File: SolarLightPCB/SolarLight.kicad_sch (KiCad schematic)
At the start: 19 parts, among them J1 I2C, J2 SPI, J3 SCK Jumper, J4 ADC, U1 TP4056, U2 WeMos_D1_mini, U3 L78L33_TO92

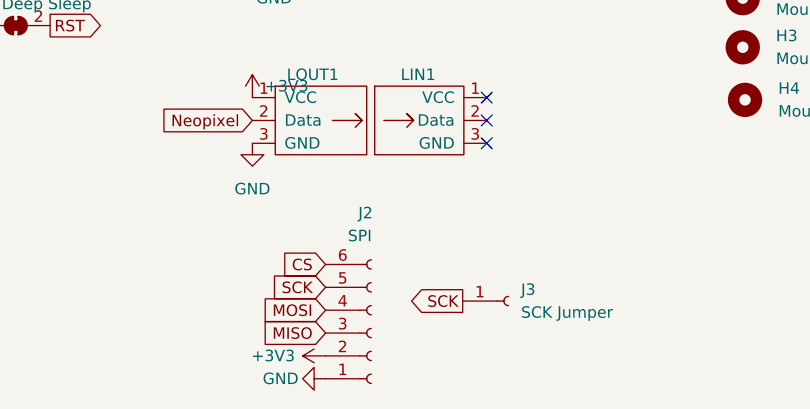
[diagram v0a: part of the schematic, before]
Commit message: Replace the missing connection with a jumper
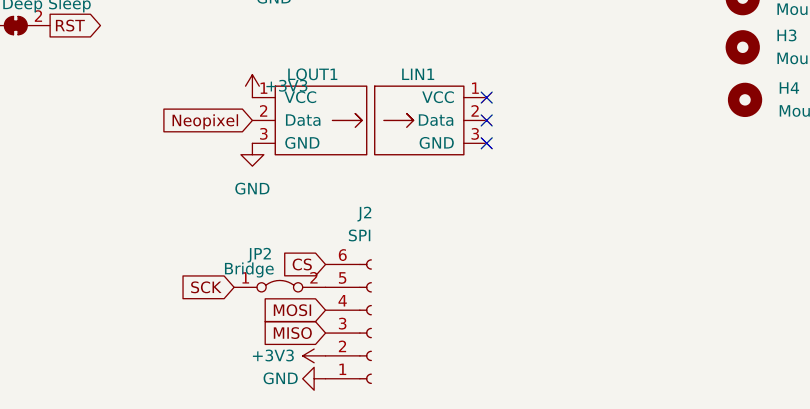
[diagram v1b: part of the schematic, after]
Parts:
- removed J3: SCK Jumper, Connector_PinHeader_2.54mm:PinHeader_1x01_P2.54mm_Vertical, symbol Connector:Conn_01x01_Female
- added JP2: Bridge, Resistor_THT:R_Box_L8.4mm_W2.5mm_P5.08mm, symbol Jumper:Jumper_2_Bridged
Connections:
- net SCK: now also JP2.1 (A); no longer J2.5 (Pin_5)
- new net: J2.5 (Pin_5), JP2.2 (B)
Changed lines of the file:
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@@
-    )
-  )
-  (global_label "SCK" (shape output) (at 234.823 117.602 180) (fields_autoplaced)
-    (effects (font (size 1.27 1.27)) (justify right))
-    (property "Intersheet References" "${INTERSHEET_REFS}" (id 0) (at 228.6604 117.6814 0)
-      (effects (font (size 1.27 1.27)) (justify right) hide)
     )
   )
@@
     )
   )
-  (global_label "SCK" (shape input) (at 219.583 116.078 180) (fields_autoplaced)
+  (global_label "SCK" (shape input) (at 209.423 116.078 180) (fields_autoplaced)
     (effects (font (size 1.27 1.27)) (justify right))
-    (property "Intersheet References" "${INTERSHEET_REFS}" (id 0) (at 213.4204 115.9986 0)
+    (property "Intersheet References" "${INTERSHEET_REFS}" (id 0) (at 203.2604 115.9986 0)
       (effects (font (size 1.27 1.27)) (justify right) hide)
     )
@@
     )
     (pin "1")
+  )
+  (symbol (lib_id "Jumper:Jumper_2_Bridged") (at 214.503 116.078 0) (unit 1)
+    (in_bom yes) (on_board yes)
+    (property "Reference" "JP2" (id 0) (at 212.344 112.395 0))
+    (property "Value" "Bridge" (id 1) (at 211.074 114.046 0))
+    (property "Footprint" "Resistor_THT:R_Box_L8.4mm_W2.5mm_P5.08mm" (id 2) (at 214.503 116.078 0)
+      (effects (font (size 1.27 1.27)) hide)
+    )
+    (property "Datasheet" "~" (id 3) (at 214.503 116.078 0)
+      (effects (font (size 1.27 1.27)) hide)
+    )
+    (pin "1")
+    (pin "2")
   )
   (symbol (lib_id "Mechanical:MountingHole") (at 265.938 83.947 0) (unit 1)
@@
     (pin "3")
   )
-  (symbol (lib_id "Connector:Conn_01x01_Female") (at 239.903 117.602 0) (unit 1)
-    (in_bom yes) (on_board yes)
-    (property "Reference" "J3" (id 0) (at 241.3 116.3319 0)
-      (effects (font (size 1.27 1.27)) (justify left))
-    )
-    (property "Value" "SCK Jumper" (id 1) (at 241.3 118.8719 0)
-      (effects (font (size 1.27 1.27)) (justify left))
-    )
-    (property "Footprint" "Connector_PinHeader_2.54mm:PinHeader_1x01_P2.54mm_Vertical" (id 2) (at 239.903 117.602 0)
-      (effects (font (size 1.27 1.27)) hide)
-    )
-    (property "Datasheet" "~" (id 3) (at 239.903 117.602 0)
-      (effects (font (size 1.27 1.27)) hide)
-    )
-    (pin "1")
-  )
   (symbol (lib_id "Device:C_Polarized") (at 146.685 33.02 0) (unit 1)
     (in_bom yes) (on_board yes) (fields_autoplaced)
@@
       (reference "J2") (unit 1) (value "SPI") (footprint "Connector_PinHeader_2.54mm:PinHeader_1x06_P2.54mm_Vertical")
     )
-    (path "/e53f4b10-ac86-4ea2-bd5b-912502e02f22"
-      (reference "J3") (unit 1) (value "SCK Jumper") (footprint "Connector_PinHeader_2.54mm:PinHeader_1x01_P2.54mm_Vertical")
-    )
     (path "/ba03d50b-1a69-484f-aaa5-388057035199"
       (reference "J4") (unit 1) (value "ADC") (footprint "Connector_PinHeader_2.54mm:PinHeader_1x01_P2.54mm_Vertical")
@@
       (reference "JP1") (unit 1) (value "Deep Sleep") (footprint "Jumper:SolderJumper-2_P1.3mm_Bridged_Pad1.0x1.5mm")
     )
+    (path "/a04ab534-b3ff-41d2-b40f-b10866f1afa8"
+      (reference "JP2") (unit 1) (value "Bridge") (footprint "Resistor_THT:R_Box_L8.4mm_W2.5mm_P5.08mm")
+    )
     (path "/efe1edb9-34c9-473f-839b-20e06ddf294c"

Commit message: Update schematic
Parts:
- U3: value L78L33_TO92 -> MCP1700-3302E
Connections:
- net ADC: no longer names the net of J4.1 (Pin_1), U2.2 (A0)
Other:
- company: (none) -> Fablab Zürich / Beat Besmer / Bernd Heistercamp
- title: (none) -> Solar Light
- moved on the sheet: J4
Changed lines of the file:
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@@
 (kicad_sch (version 20211123) (generator eeschema)
   (paper "A4")
+  (title_block
+    (title "Solar Light")
+    (date "2022-10-23")
+    (rev "v0.1")
+    (company "Fablab Zürich / Beat Besmer / Bernd Heistercamp")
+  )
   (junction (at 74.93 40.64) (diameter 0) (color 0 0 0 0)
   )
@@
     )
   )
-  (global_label "ADC" (shape output) (at 169.926 67.056 180) (fields_autoplaced)
-    (effects (font (size 1.27 1.27)) (justify right))
-    (property "Intersheet References" "${INTERSHEET_REFS}" (id 0) (at 163.8843 66.9766 0)
-      (effects (font (size 1.27 1.27)) (justify right) hide)
-    )
-  )
   (global_label "CS" (shape input) (at 219.583 113.538 180) (fields_autoplaced)
     (effects (font (size 1.27 1.27)) (justify right))
@@
     )
   )
-  (global_label "ADC" (shape input) (at 171.45 84.455 0) (fields_autoplaced)
-    (effects (font (size 1.27 1.27)) (justify left))
-    (property "Intersheet References" "${INTERSHEET_REFS}" (id 0) (at 177.4917 84.3756 0)
-      (effects (font (size 1.27 1.27)) (justify left) hide)
-    )
-  )
   (global_label "Neopixel" (shape input) (at 211.455 97.536 180) (fields_autoplaced)
     (effects (font (size 1.27 1.27)) (justify right))
@@
   (symbol (lib_id "Device:Battery_Cell") (at 118.745 38.1 0) (unit 1)
     (in_bom yes) (on_board yes)
-    (property "Reference" "BT1" (id 0) (at 122.555 34.7979 0)
+    (property "Reference" "BT1" (id 0) (at 119.507 39.116 0)
       (effects (font (size 1.27 1.27)) (justify left))
     )
     (property "Value" "Battery_Cell" (id 1) (at 113.03 42.545 0)
-      (effects (font (size 1.27 1.27)) (justify left))
+      (effects (font (size 1.27 1.27)) (justify left) hide)
     )
     (property "Footprint" "Resistor_THT:R_Axial_DIN0207_L6.3mm_D2.5mm_P10.16mm_Horizontal" (id 2) (at 118.745 36.576 90)
@@
   )
   (symbol (lib_id "Device:Solar_Cell") (at 74.93 36.83 0) (unit 1)
-    (in_bom yes) (on_board yes) (fields_autoplaced)
+    (in_bom yes) (on_board yes)
     (property "Reference" "SC1" (id 0) (at 78.74 33.4009 0)
-      (effects (font (size 1.27 1.27)) (justify left))
-    )
-    (property "Value" "Solar_Cell" (id 1) (at 78.74 35.9409 0)
+      (effects (font (size 1.27 1.27)) (justify left) hide)
+    )
+    (property "Value" "Solar_Cell" (id 1) (at 63.627 37.846 0)
       (effects (font (size 1.27 1.27)) (justify left))
     )
@@
   )
   (symbol (lib_id "power:+3V3") (at 139.7 30.48 0) (unit 1)
-    (in_bom yes) (on_board yes) (fields_autoplaced)
+    (in_bom yes) (on_board yes)
     (property "Reference" "#PWR0104" (id 0) (at 139.7 34.29 0)
       (effects (font (size 1.27 1.27)) hide)
     )
-    (property "Value" "+3V3" (id 1) (at 139.7 25.4 0))
+    (property "Value" "+3V3" (id 1) (at 142.494 27.686 0))
     (property "Footprint" "" (id 2) (at 139.7 30.48 0)
       (effects (font (size 1.27 1.27)) hide)
@@
   )
   (symbol (lib_id "Regulator_Linear:L78L33_TO92") (at 132.08 30.48 0) (unit 1)
-    (in_bom yes) (on_board yes) (fields_autoplaced)
-    (property "Reference" "U3" (id 0) (at 132.08 22.86 0))
-    (property "Value" "L78L33_TO92" (id 1) (at 132.08 25.4 0))
+    (in_bom yes) (on_board yes)
+    (property "Reference" "U3" (id 0) (at 132.08 27.432 0))
+    (property "Value" "MCP1700-3302E" (id 1) (at 132.08 25.4 0))
     (property "Footprint" "Package_TO_SOT_THT:TO-92_Inline" (id 2) (at 132.08 24.765 0)
       (effects (font (size 1.27 1.27) italic) hide)
@@
     (pin "4")
   )
-  (symbol (lib_id "Connector:Conn_01x01_Female") (at 175.006 67.056 0) (unit 1)
-    (in_bom yes) (on_board yes)
-    (property "Reference" "J4" (id 0) (at 176.403 65.7859 0)
-      (effects (font (size 1.27 1.27)) (justify left))
-    )
-    (property "Value" "ADC" (id 1) (at 176.403 68.3259 0)
-      (effects (font (size 1.27 1.27)) (justify left))
-    )
-    (property "Footprint" "Connector_PinHeader_2.54mm:PinHeader_1x01_P2.54mm_Vertical" (id 2) (at 175.006 67.056 0)
-      (effects (font (size 1.27 1.27)) hide)
-    )
-    (property "Datasheet" "~" (id 3) (at 175.006 67.056 0)
+  (symbol (lib_id "Connector:Conn_01x01_Female") (at 176.53 84.455 0) (unit 1)
+    (in_bom yes) (on_board yes)
+    (property "Reference" "J4" (id 0) (at 175.641 80.518 0)
+      (effects (font (size 1.27 1.27)) (justify left))
+    )
+    (property "Value" "ADC" (id 1) (at 175.133 82.423 0)
+      (effects (font (size 1.27 1.27)) (justify left))
+    )
+    (property "Footprint" "Connector_PinHeader_2.54mm:PinHeader_1x01_P2.54mm_Vertical" (id 2) (at 176.53 84.455 0)
+      (effects (font (size 1.27 1.27)) hide)
+    )
+    (property "Datasheet" "~" (id 3) (at 176.53 84.455 0)
       (effects (font (size 1.27 1.27)) hide)
     )
@@
   )
   (symbol (lib_id "MCU_Module:WeMos_D1_mini") (at 161.29 97.155 0) (unit 1)
-    (in_bom yes) (on_board yes) (fields_autoplaced)
+    (in_bom yes) (on_board yes)
     (property "Reference" "U2" (id 0) (at 163.3094 117.221 0)
       (effects (font (size 1.27 1.27)) (justify left))
     )
-    (property "Value" "WeMos_D1_mini" (id 1) (at 163.3094 119.761 0)
+    (property "Value" "WeMos_D1_mini" (id 1) (at 154.178 71.628 0)
       (effects (font (size 1.27 1.27)) (justify left))
     )
@@
       (effects (font (size 1.27 1.27)) hide)
     )
-    (property "Value" "+3V3" (id 1) (at 215.265 93.726 0))
+    (property "Value" "+3V3" (id 1) (at 210.566 91.313 0))
     (property "Footprint" "" (id 2) (at 211.455 94.996 0)
       (effects (font (size 1.27 1.27)) hide)
@@
   )
   (symbol (lib_id "Device:C_Polarized") (at 146.685 33.02 0) (unit 1)
-    (in_bom yes) (on_board yes) (fields_autoplaced)
-    (property "Reference" "C1" (id 0) (at 150.495 30.8609 0)
+    (in_bom yes) (on_board yes)
+    (property "Reference" "C1" (id 0) (at 151.003 33.02 0)
       (effects (font (size 1.27 1.27)) (justify left))
     )
     (property "Value" "C_Polarized" (id 1) (at 150.495 33.4009 0)
-      (effects (font (size 1.27 1.27)) (justify left))
+      (effects (font (size 1.27 1.27)) (justify left) hide)
     )
     (property "Footprint" "Capacitor_THT:CP_Radial_D5.0mm_P2.00mm" (id 2) (at 147.6502 36.83 0)
@@
     )
     (path "/6732d4fc-02ff-4210-8868-4a455e8eb581"
-      (reference "U3") (unit 1) (value "L78L33_TO92") (footprint "Package_TO_SOT_THT:TO-92_Inline")
-    )
-  )
+      (reference "U3") (unit 1) (value "MCP1700-3302E") (footprint "Package_TO_SOT_THT:TO-92_Inline")
+    )
+  )

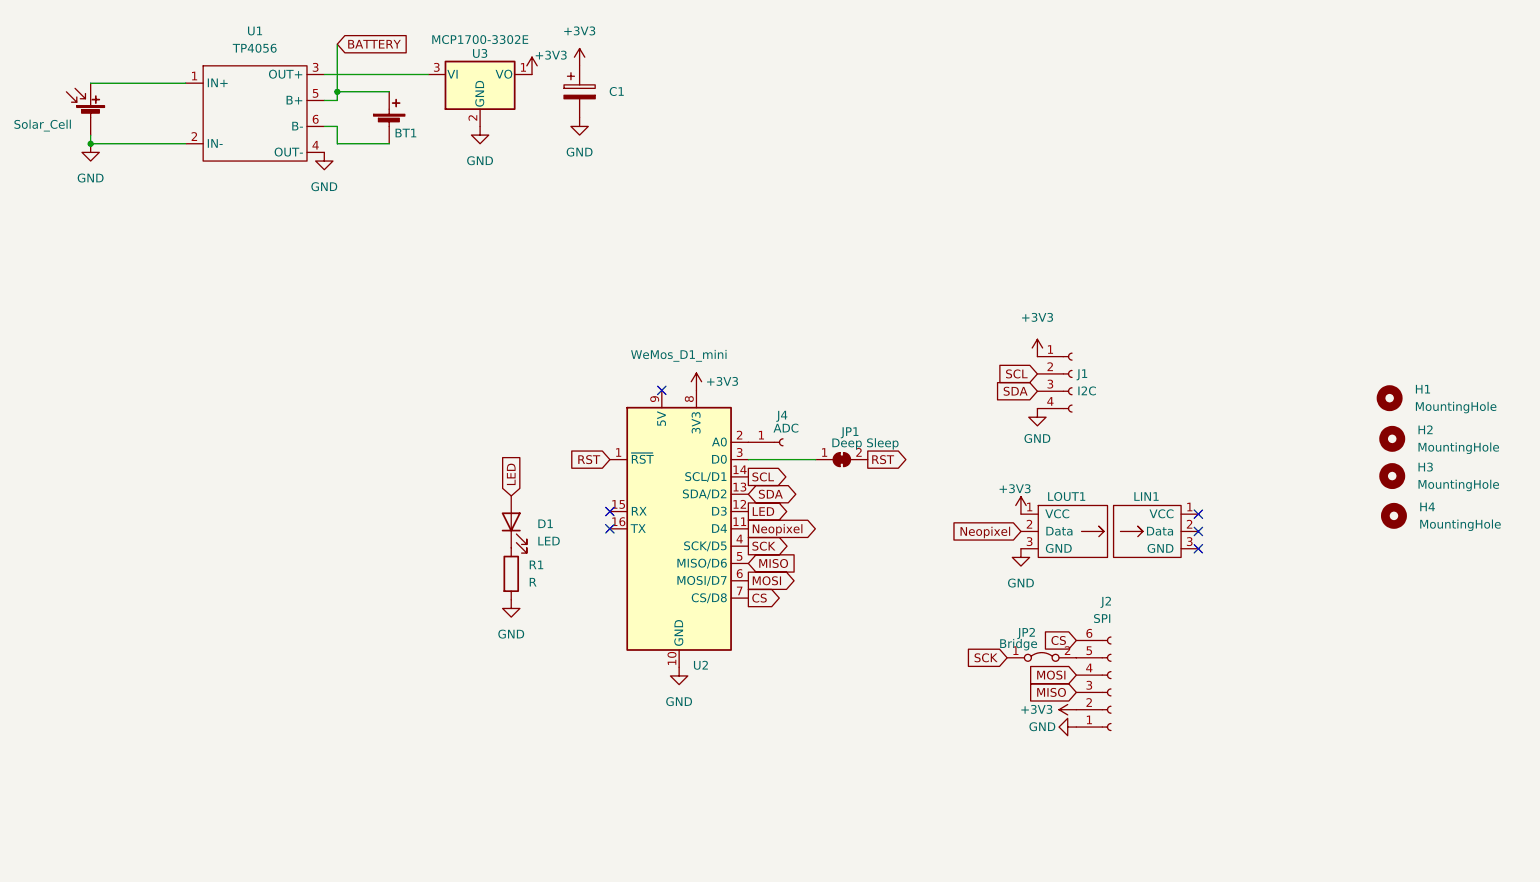
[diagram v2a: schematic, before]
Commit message: Add voltage divider to measure the battery voltage
fixes #4
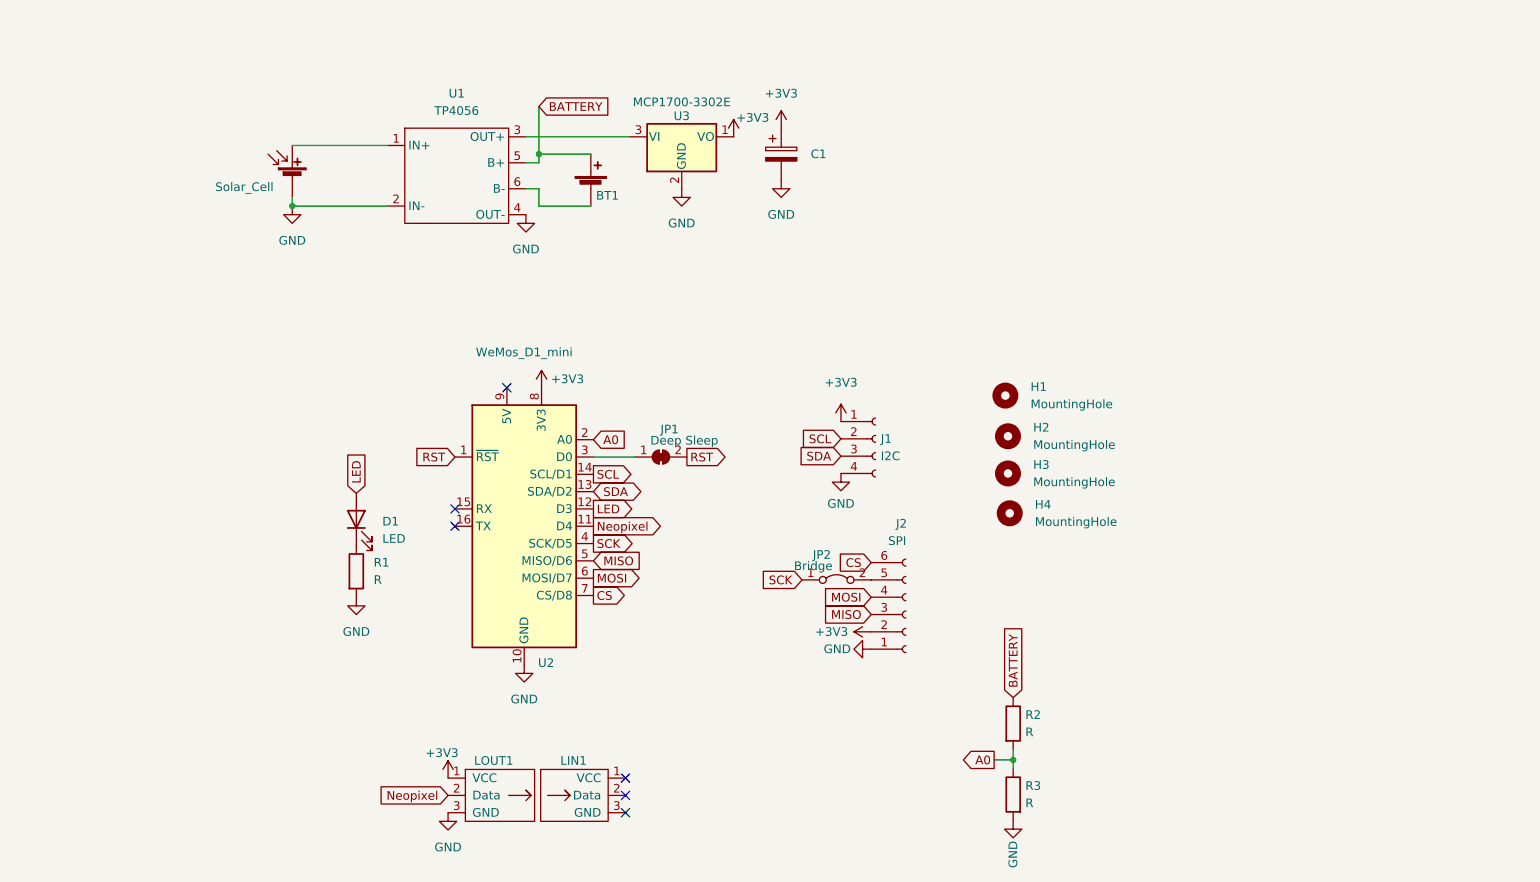
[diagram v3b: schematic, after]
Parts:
- removed J4: ADC, Connector_PinHeader_2.54mm:PinHeader_1x01_P2.54mm_Vertical, symbol Connector:Conn_01x01_Female
- added R2, R3: R, Resistor_THT:R_Axial_DIN0207_L6.3mm_D2.5mm_P7.62mm_Horizontal, symbol Device:R
- BT1: footprint Resistor_THT:R_Axial_DIN0207_L6.3mm_D2.5mm_P10.16mm_Horizontal -> Connector_PinHeader_2.54mm:PinHeader_1x02_P2.54mm_Vertical
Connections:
- net BATTERY: now also R2.1
- net GND: now also R3.2
- net A0: now reaches U2.2 (A0)
- net A0: now also R2.2, R3.1
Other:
- moved on the sheet: BT1, C1, D1, H1, H2, H3, H4, J1, J2, JP1, JP2, LIN1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
